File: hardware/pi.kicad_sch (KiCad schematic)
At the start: 59 parts, among them SW1 BOOTSEL, SW2 RESET, U10 RP2040, U11 SS54_C22452, U12 SS54_C22452, U13 CAN_IO, U14 TJA1042T_3_1J, U15 USB-C, U5 NCP1117ST33T3G, U6 SKCR-16S, U7 WS2812E-V5, U8 W25Q128JVSIQ, U9 74HC165D,653, X1 12MHz

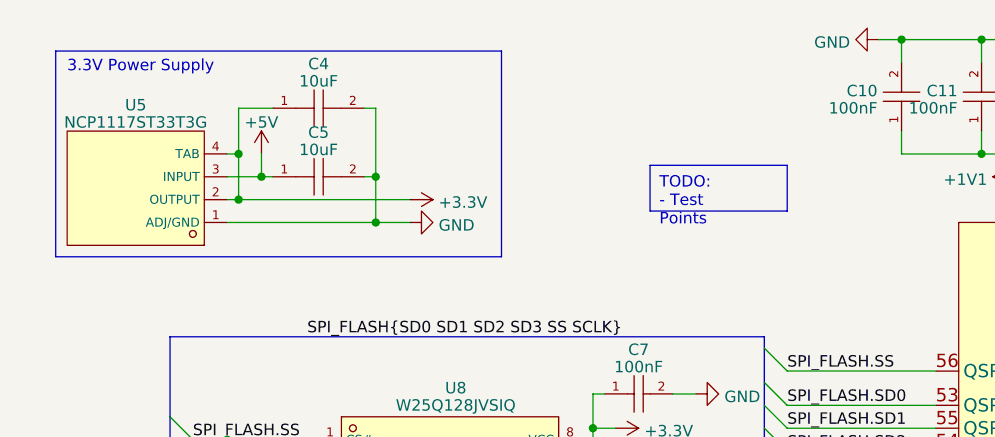
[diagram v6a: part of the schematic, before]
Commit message: replace 3.3v ldo with in-stock part
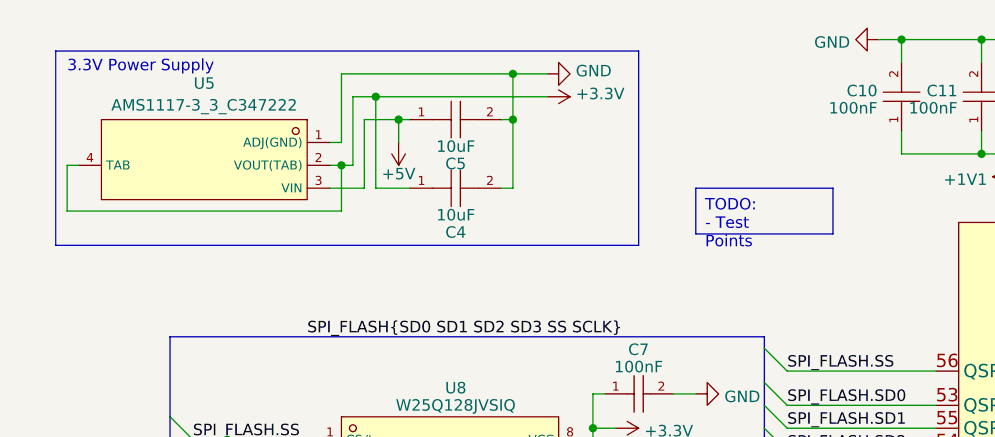
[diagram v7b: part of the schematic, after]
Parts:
- removed U5: NCP1117ST33T3G, jlc_footprints:SOT-223-3_L6.5-W3.4-P2.30-LS7.0-BR, symbol jlc:NCP1117ST33T3G
- added U5: AMS1117-3_3_C347222, jlc_footprints:SOT-223-4_L6.5-W3.5-P2.30-LS7.0-BR, symbol jlc:AMS1117-3_3_C347222
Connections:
- net +3.3V: now also U5.2 (VOUT(TAB)), U5.4 (TAB)
- net +5V: now also U5.3 (VIN)
- net GND: now also U5.1 (ADJ(GND))
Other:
- moved on the sheet: C4, C5

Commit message: make svgs in docs interactive
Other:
- sheet 5V PSU renamed PI_PSU
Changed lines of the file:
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@@
     (stroke (width 0.1524) (type solid))
     (fill (color 0 0 0 0.0000))
-    (property "Sheetname" "5V PSU" (at 125.73 155.4984 0)
+    (property "Sheetname" "PI_PSU" (at 125.73 155.4984 0)
       (effects (font (size 1.27 1.27)) (justify left bottom))
     )
